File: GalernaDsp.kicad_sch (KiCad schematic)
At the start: 0 parts

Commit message: Audio schematic updated
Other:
- sheet Audio Codec renamed Audio
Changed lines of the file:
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@@
 	)
 	(sheet
-		(at 82.55 109.22)
+		(at 81.788 90.678)
 		(size 36.83 21.59)
 		(exclude_from_sim no)
@@
 		)
 		(property "Sheetname" "Power"
-			(at 82.55 106.6034 0)
+			(at 81.788 88.0614 0)
 			(effects
 				(font
@@
 		)
 		(property "Sheetfile" "power.kicad_sch"
-			(at 82.55 131.3946 0)
+			(at 81.788 112.8526 0)
 			(effects
 				(font
@@
 			(color 0 0 0 0.0000)
 		)
-		(property "Sheetname" "Audio Codec"
+		(property "Sheetname" "Audio"
 			(at 140.97 51.9934 0)
 			(effects

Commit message: extending library
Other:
- added sheet Input Control (input_control.kicad_sch)
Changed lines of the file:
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@@
 				(font
 					(size 5.08 5.08)
-					(thickness 1.016)
-					(bold yes)
+					(thickness 0.635)
 				)
 				(justify left bottom)
@@
 				)
 			)
+		)
+	)
+	(sheet
+		(at 144.78 91.44)
+		(size 40.64 20.32)
+		(exclude_from_sim no)
+		(in_bom yes)
+		(on_board yes)
+		(dnp no)
+		(fields_autoplaced yes)
+		(stroke
+			(width 0.1524)
+			(type solid)
+		)
+		(fill
+			(color 0 0 0 0.0000)
+		)
+		(property "Sheetname" "Input Control"
+			(at 144.78 88.8234 0)
+			(effects
+				(font
+					(size 5.08 5.08)
+					(thickness 1.016)
+					(bold yes)
+				)
+				(justify left bottom)
+			)
+		)
+		(property "Sheetfile" "input_control.kicad_sch"
+			(at 144.78 112.3446 0)
+			(effects
+				(font
+					(size 1.27 1.27)
+				)
+				(justify left top)
+			)
+		)
+		(instances
+			(project "GalernaDsp"
+				(path "/a77f8f1b-3e6d-40f9-a36e-54a20299e9bc"
+					(page "5")
+				)
+			)

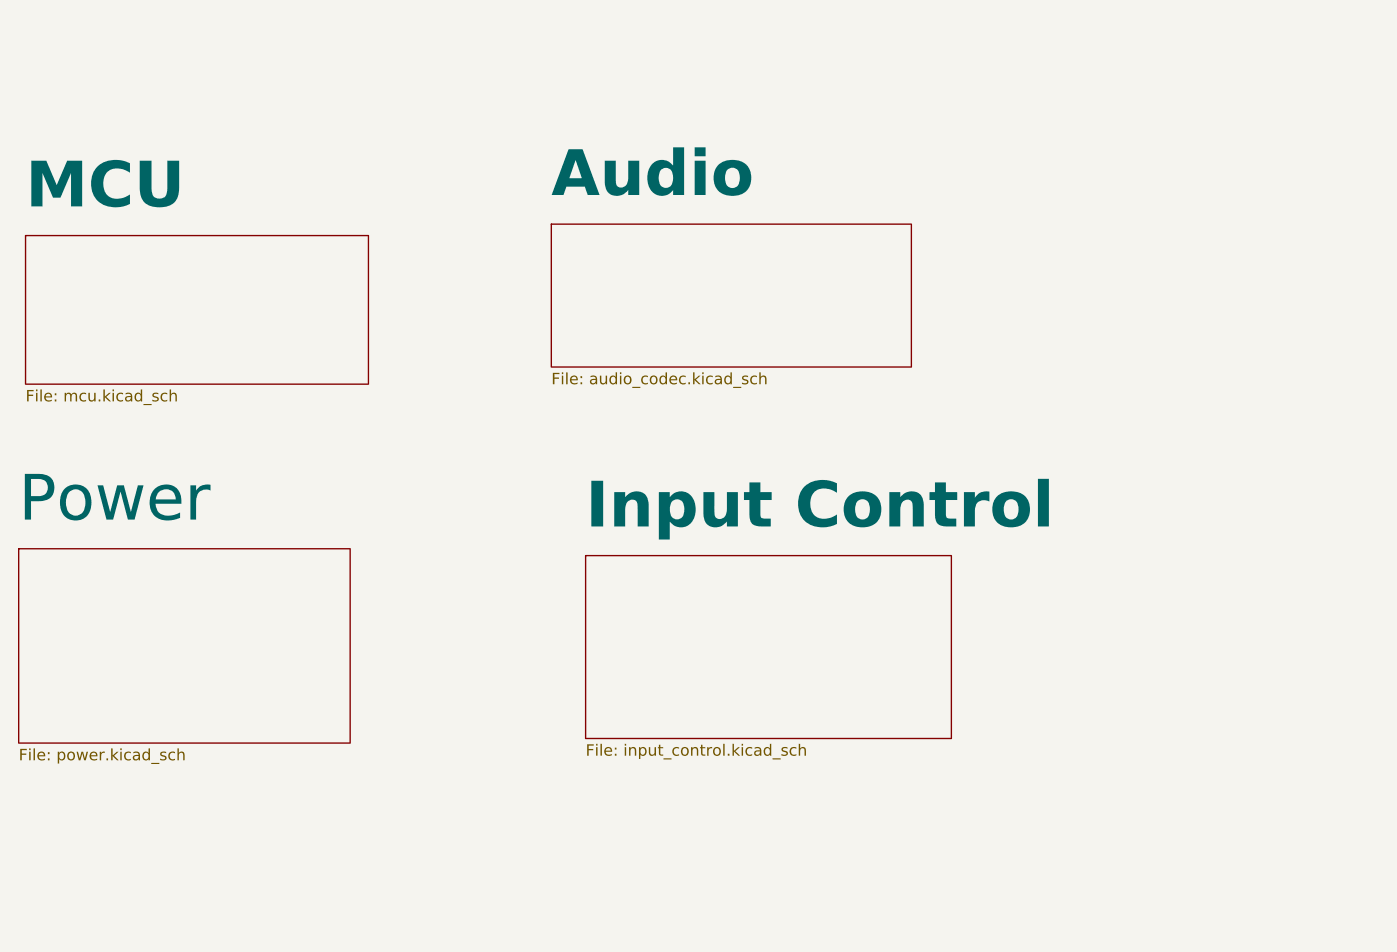
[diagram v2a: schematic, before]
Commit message: footprints updated
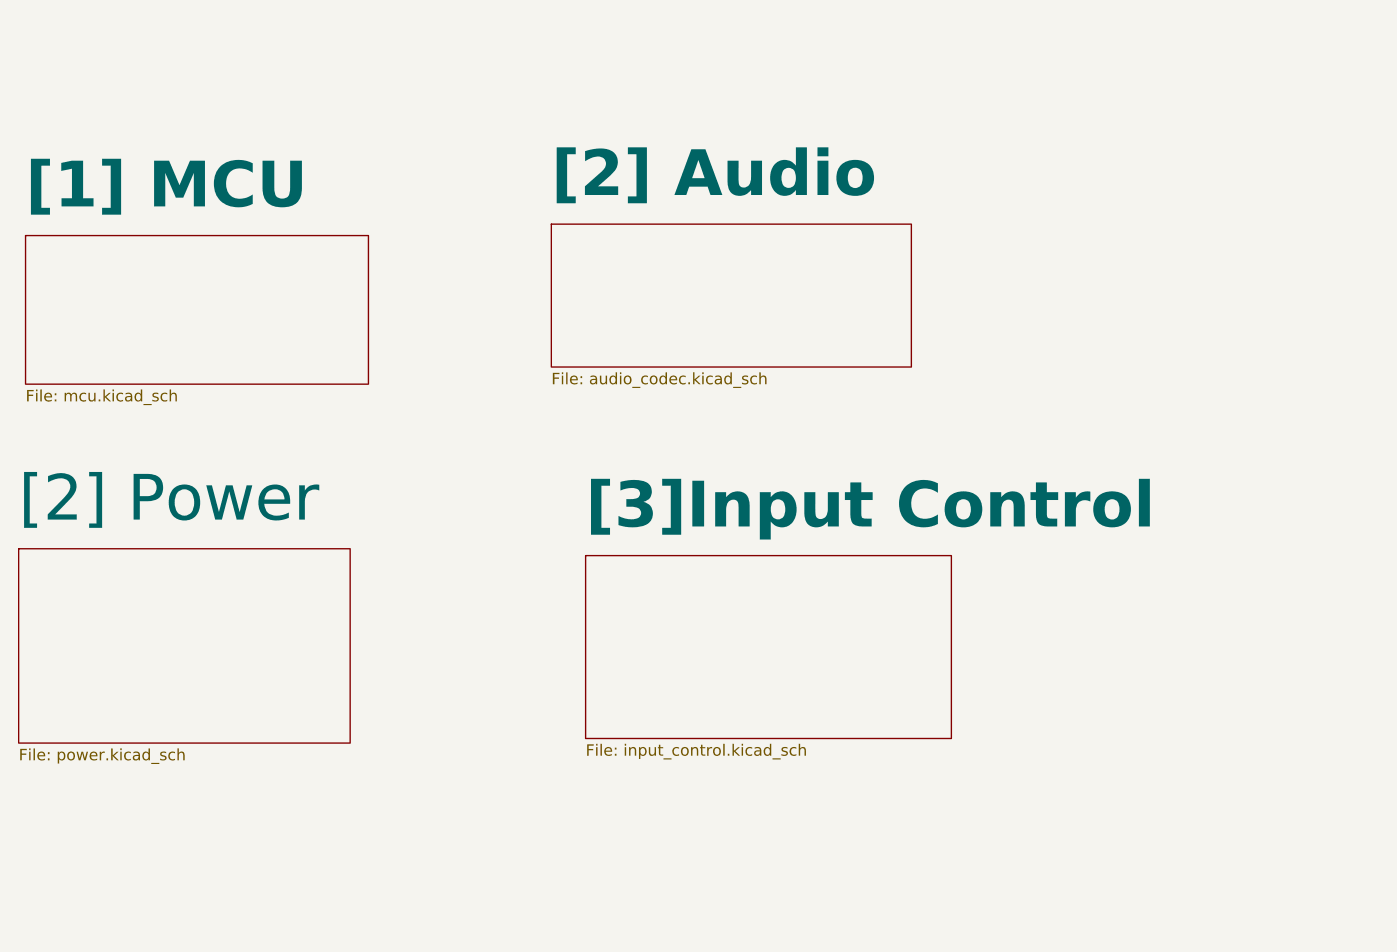
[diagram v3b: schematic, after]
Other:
- sheet Audio renamed [2] Audio
- sheet Input Control renamed [3]Input Control
- sheet MCU renamed [1] MCU
- sheet Power renamed [2] Power
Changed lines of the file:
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@@
 			(color 0 0 0 0.0000)
 		)
-		(property "Sheetname" "Power"
+		(property "Sheetname" "[2] Power"
 			(at 81.788 88.0614 0)
 			(effects
@@
 			(color 0 0 0 0.0000)
 		)
-		(property "Sheetname" "MCU"
+		(property "Sheetname" "[1] MCU"
 			(at 82.55 53.2634 0)
 			(effects
@@
 			(color 0 0 0 0.0000)
 		)
-		(property "Sheetname" "Input Control"
+		(property "Sheetname" "[3]Input Control"
 			(at 144.78 88.8234 0)
 			(effects
@@
 			(color 0 0 0 0.0000)
 		)
-		(property "Sheetname" "Audio"
+		(property "Sheetname" "[2] Audio"
 			(at 140.97 51.9934 0)
 			(effects

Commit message: pcb setup
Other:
- sheet [3]Input Control renamed [3] Input Control
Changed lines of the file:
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@@
 			(color 0 0 0 0.0000)
 		)
-		(property "Sheetname" "[3]Input Control"
+		(property "Sheetname" "[3] Input Control"
 			(at 144.78 88.8234 0)
 			(effects

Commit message: updating names
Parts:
- added H000, H001, H002, H003: MountingHole, MountingHole:MountingHole_2.5mm, symbol Mechanical:MountingHole

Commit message: net classes added
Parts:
- H000, H001, H002, H003: footprint MountingHole:MountingHole_2.5mm -> MountingHole:MountingHole_3.2mm_M3_DIN965_Pad_TopBottom
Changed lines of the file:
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@@
 			)
 		)
-		(property "Footprint" "MountingHole:MountingHole_2.5mm"
+		(property "Footprint" "MountingHole:MountingHole_3.2mm_M3_DIN965_Pad_TopBottom"
 			(at 214.63 41.91 0)
 			(effects
@@
 			)
 		)
-		(property "Footprint" "MountingHole:MountingHole_2.5mm"
+		(property "Footprint" "MountingHole:MountingHole_3.2mm_M3_DIN965_Pad_TopBottom"
 			(at 214.63 34.29 0)
 			(effects
@@
 			)
 		)
-		(property "Footprint" "MountingHole:MountingHole_2.5mm"
+		(property "Footprint" "MountingHole:MountingHole_3.2mm_M3_DIN965_Pad_TopBottom"
 			(at 214.63 49.53 0)
 			(effects
@@
 	(symbol
 		(lib_id "Mechanical:MountingHole")
-		(at 214.63 57.15 0)
+		(at 214.63 58.42 0)
 		(unit 1)
 		(exclude_from_sim no)
@@
 		(fields_autoplaced yes)
 		(property "Reference" "H003"
-			(at 217.17 55.8799 0)
+			(at 217.17 57.1499 0)
 			(effects
 				(font
@@
 		)
 		(property "Value" "MountingHole"
-			(at 217.17 58.4199 0)
-			(effects
-				(font
-					(size 1.27 1.27)
-				)
-				(justify left)
-			)
-		)
-		(property "Footprint" "MountingHole:MountingHole_2.5mm"
-			(at 214.63 57.15 0)
-			(effects
-				(font
-					(size 1.27 1.27)
-				)
-				(hide yes)
-			)
-		)
-		(property "Datasheet" "~"
-			(at 214.63 57.15 0)
-			(effects
-				(font
-					(size 1.27 1.27)
-				)
-				(hide yes)
-			)
-		)
-		(property "Description" "Mounting Hole without connection"
-			(at 214.63 57.15 0)
-			(effects
-				(font
+			(at 217.17 59.6899 0)
+			(effects
+				(font
+					(size 1.27 1.27)
+				)
+				(justify left)
+			)
+		)
+		(property "Footprint" "MountingHole:MountingHole_3.2mm_M3_DIN965_Pad_TopBottom"
+			(at 214.63 58.42 0)
+			(effects
+				(font
+					(size 1.27 1.27)
+				)
+				(hide yes)
+			)
+		)
+		(property "Datasheet" "~"
+			(at 214.63 58.42 0)
+			(effects
+				(font
+					(size 1.27 1.27)
+				)
+				(hide yes)
+			)
+		)
+		(property "Description" "Mounting Hole without connection"
+			(at 214.63 58.42 0)
+			(effects
+				(font

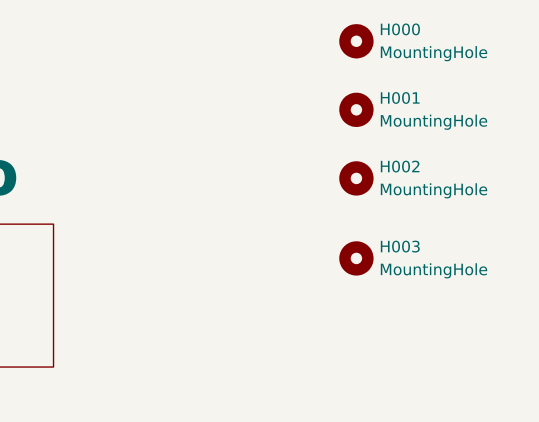
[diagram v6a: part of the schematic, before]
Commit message: Codec updated to ES8388 on schematic
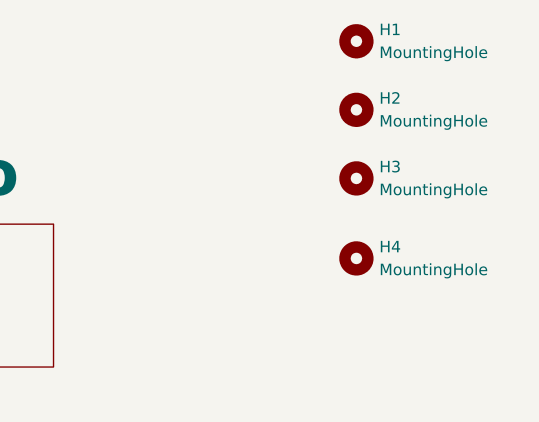
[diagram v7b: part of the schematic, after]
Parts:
- renumbered H000 to H1, H001 to H2, H002 to H3, H003 to H4
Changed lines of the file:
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@@
 		(dnp no)
 		(fields_autoplaced yes)
-		(property "Reference" "H001"
+		(property "Reference" "H2"
 			(at 217.17 40.6399 0)
 			(effects
@@
 			(project "GalernaDsp"
 				(path "/a77f8f1b-3e6d-40f9-a36e-54a20299e9bc"
-					(reference "H001")
+					(reference "H2")
 					(unit 1)
 				)
@@
 		(dnp no)
 		(fields_autoplaced yes)
-		(property "Reference" "H000"
+		(property "Reference" "H1"
 			(at 217.17 33.0199 0)
 			(effects
@@
 			(project ""
 				(path "/a77f8f1b-3e6d-40f9-a36e-54a20299e9bc"
-					(reference "H000")
+					(reference "H1")
 					(unit 1)
 				)
@@
 		(dnp no)
 		(fields_autoplaced yes)
-		(property "Reference" "H002"
+		(property "Reference" "H3"
 			(at 217.17 48.2599 0)
 			(effects
@@
 			(project "GalernaDsp"
 				(path "/a77f8f1b-3e6d-40f9-a36e-54a20299e9bc"
-					(reference "H002")
+					(reference "H3")
 					(unit 1)
 				)
@@
 		(dnp no)
 		(fields_autoplaced yes)
-		(property "Reference" "H003"
+		(property "Reference" "H4"
 			(at 217.17 57.1499 0)
 			(effects
@@
 			(project "GalernaDsp"
 				(path "/a77f8f1b-3e6d-40f9-a36e-54a20299e9bc"
-					(reference "H003")
-					(unit 1)
-				)
+					(reference "H4")
+					(unit 1)
+				)
